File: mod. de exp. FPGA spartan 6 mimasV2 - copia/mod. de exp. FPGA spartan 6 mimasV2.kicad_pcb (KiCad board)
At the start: 2 copper layers, 111.5 x 57.8 mm, 46 parts, among them J1 locked, J2 locked, J3 locked, J4 locked, SW1 SW_DIP_x08, SW2 SW_Push, SW3 SW_Push, SW4 SW_Push, SW5 SW_Push, U1 CA56-12CGKWA

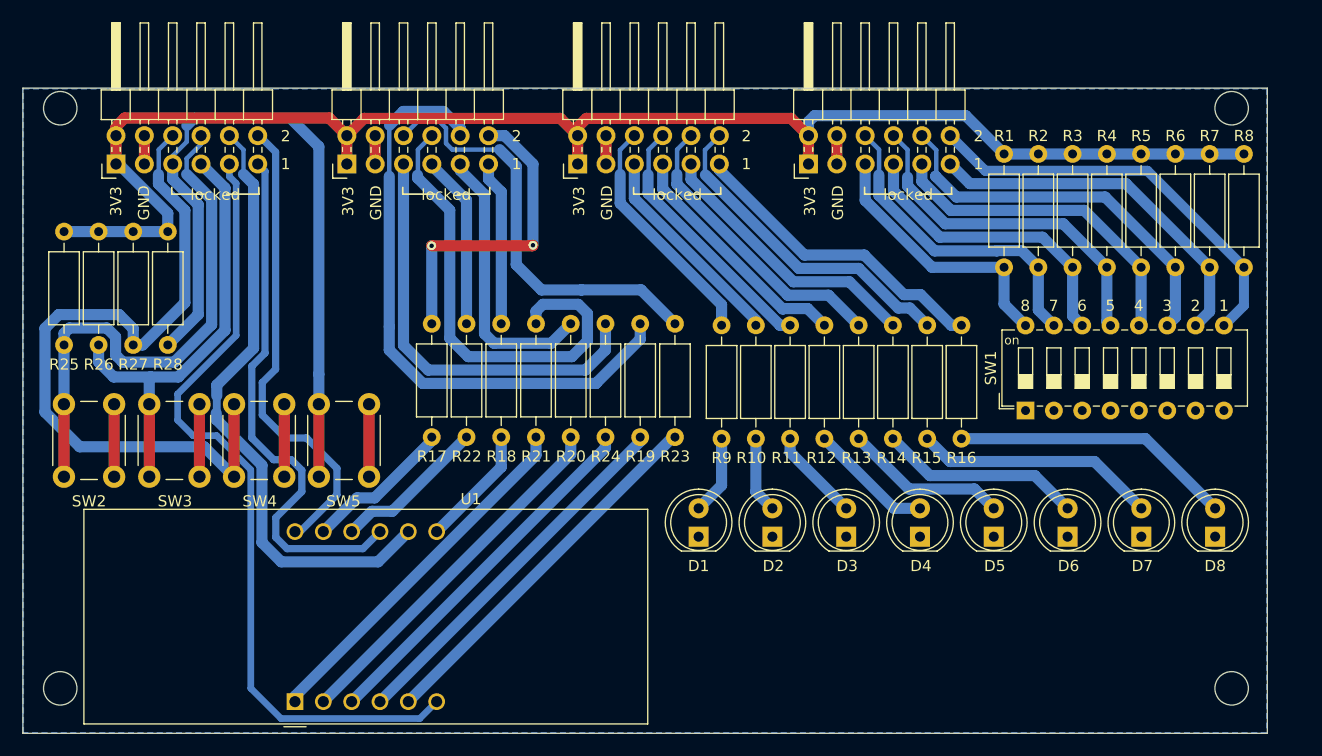
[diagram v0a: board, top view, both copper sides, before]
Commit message: el THT del FPGA modul
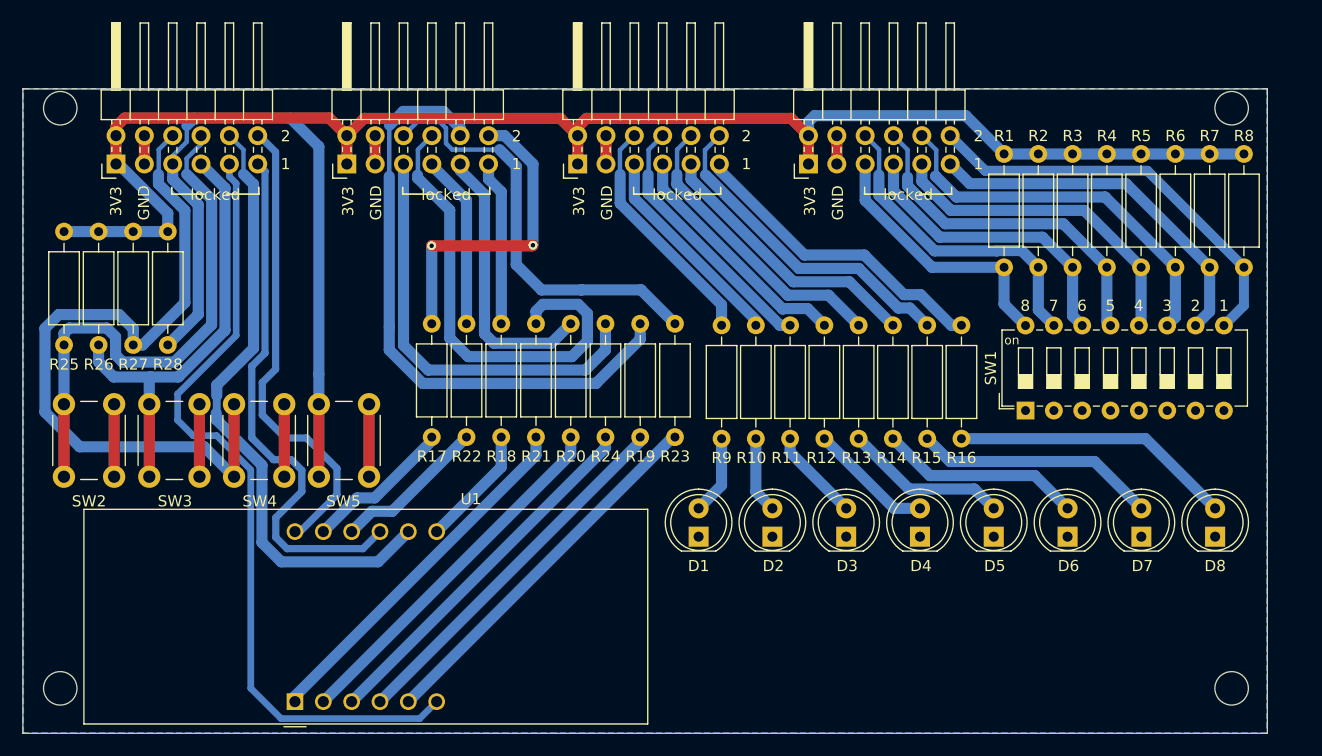
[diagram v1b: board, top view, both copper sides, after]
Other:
- outline, holes or cut-outs redrawn
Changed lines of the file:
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@@
   (gr_circle (center 200 95) (end 201.5 95) (layer "Edge.Cuts") (width 0.1) (fill none))
   (gr_circle (center 95 147) (end 96.5 147) (layer "Edge.Cuts") (width 0.1) (fill none))
-  (gr_rect (start 91.65 151.03) (end 203.2 93.2) (layer "Edge.Cuts") (width 0.1) (fill none))
+  (gr_rect (start 91.65 151.03) (end 203.2 93.27) (layer "Edge.Cuts") (width 0.1) (fill none))
   (gr_circle (center 95 95) (end 96.5 95) (layer "Edge.Cuts") (width 0.1) (fill none))
   (gr_circle (center 200 147) (end 201.5 147) (layer "Edge.Cuts") (width 0.1) (fill none))

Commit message: absolutamente todo
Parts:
- added G***: LOGO, wao:logo v2, F.Cu at (175.3, 123.0)
- R10, R11, R12, R13, R14, R15, R16, R25, R26, R27, R28, R9: footprint Resistor_THT:R_Axial_DIN0207_L6.3mm_D2.5mm_P10.16mm_Horizontal -> Resistor_THT:R_Axial_DIN0207_L6.3mm_D2.5mm_P7.62mm_Horizontal
- R17, R18, R19, R20, R21, R22, R23, R24: footprint Resistor_THT:R_Axial_DIN0207_L6.3mm_D2.5mm_P10.16mm_Horizontal -> Resistor_THT:R_Axial_DIN0207_L6.3mm_D2.5mm_P7.62mm_Horizontal; moved to B.Cu
- moved R25 26.4 mm to (110.5, 127.7)
- moved U1 26.3 mm to (110.8, 122.4)
- moved R24 24.9 mm to (119.1, 111.6)
- moved R26 23.5 mm to (107.5, 127.7)
- moved R28 21.9 mm to (101.3, 127.7)
- moved R27 21.9 mm to (104.4, 127.7)
- moved SW2 19.5 mm to (118.1, 128.4)
- moved SW4 19.5 mm to (133.3, 128.4)
- moved SW3 19.5 mm to (125.7, 128.4)
- moved SW5 19.5 mm to (140.9, 128.4)
- moved R20 15.7 mm to (125.3, 111.6)
- moved R19 12.7 mm to (134.5, 111.6)
- moved R23 9.77 mm to (140.7, 111.6)
- moved R22 9.59 mm to (122.2, 111.6)
- moved R15 9.11 mm to (163.6, 114.0)
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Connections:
- D1 pad 1: GND -> GND2
- D2 pad 1: GND -> GND2
- D3 pad 1: GND -> GND2
- D4 pad 1: GND -> GND2
- D5 pad 1: GND -> GND2
- D6 pad 1: GND -> GND2
- D7 pad 1: GND -> GND2
- D8 pad 1: GND -> GND2
- J2 pad 1: +3V3 -> +3.3V
- J2 pad 2: +3V3 -> +3.3V
- J2 pad 3: GND -> GND1
- J2 pad 4: GND -> GND1
- J3 pad 1: +3V3 -> +3.3VA
- J3 pad 2: +3V3 -> +3.3VA
- J3 pad 3: GND -> GND2
- J3 pad 4: GND -> GND2
- J4 pad 1: +3V3 -> +3.3VADC
- J4 pad 2: +3V3 -> +3.3VADC
- J4 pad 3: GND -> GND3
- J4 pad 4: GND -> GND3
- R1 pad 1: +3V3 -> +3.3VADC
- R1 pad 2: /DIP_SWITCH/7P9 -> /DIP_SWITCH/8P9
- R17 pad 1: /DISPLAY/2P7 -> /DISPLAY/1P7
- R18 pad 1: /DISPLAY/1P7 -> /DISPLAY/2P7
- R19 pad 1: /DISPLAY/4P7 -> /DISPLAY/3P7
- R2 pad 1: +3V3 -> +3.3VADC
- R2 pad 2: /DIP_SWITCH/8P9 -> /DIP_SWITCH/7P9
- R20 pad 1: /DISPLAY/3P7 -> /DISPLAY/4P7
- R21 pad 1: /DISPLAY/6P7 -> /DISPLAY/5P7
- R22 pad 1: /DISPLAY/5P7 -> /DISPLAY/6P7
- R23 pad 1: /DISPLAY/8P7 -> /DISPLAY/7P7
- R24 pad 1: /DISPLAY/7P7 -> /DISPLAY/8P7
- R3 pad 1: +3V3 -> +3.3VADC
- R3 pad 2: /DIP_SWITCH/5P9 -> /DIP_SWITCH/6P9
- R4 pad 1: +3V3 -> +3.3VADC
- R4 pad 2: /DIP_SWITCH/6P9 -> /DIP_SWITCH/5P9
- R5 pad 1: +3V3 -> +3.3VADC
- R5 pad 2: /DIP_SWITCH/3P9 -> /DIP_SWITCH/4P9
- R6 pad 1: +3V3 -> +3.3VADC
- R6 pad 2: /DIP_SWITCH/4P9 -> /DIP_SWITCH/3P9
- R7 pad 1: +3V3 -> +3.3VADC
- R7 pad 2: /DIP_SWITCH/1P9 -> /DIP_SWITCH/2P9
- R8 pad 1: +3V3 -> +3.3VADC
- R8 pad 2: /DIP_SWITCH/2P9 -> /DIP_SWITCH/1P9
- SW1 pad 1: GND -> GND3
- SW1 pad 10: /DIP_SWITCH/1P9 -> /DIP_SWITCH/2P9
- SW1 pad 11: /DIP_SWITCH/4P9 -> /DIP_SWITCH/3P9
- SW1 pad 12: /DIP_SWITCH/3P9 -> /DIP_SWITCH/4P9
- SW1 pad 13: /DIP_SWITCH/6P9 -> /DIP_SWITCH/5P9
- SW1 pad 14: /DIP_SWITCH/5P9 -> /DIP_SWITCH/6P9
- SW1 pad 15: /DIP_SWITCH/8P9 -> /DIP_SWITCH/7P9
- SW1 pad 16: /DIP_SWITCH/7P9 -> /DIP_SWITCH/8P9
- SW1 pad 2: GND -> GND3
- SW1 pad 3: GND -> GND3
- SW1 pad 4: GND -> GND3
- SW1 pad 5: GND -> GND3
- SW1 pad 6: GND -> GND3
- SW1 pad 7: GND -> GND3
- SW1 pad 8: GND -> GND3
- SW1 pad 9: /DIP_SWITCH/2P9 -> /DIP_SWITCH/1P9
- SW2 pad 1: GND -> GND2
- SW3 pad 1: GND -> GND2
- SW4 pad 1: GND -> GND2
- SW5 pad 1: GND -> GND2
- U1 pad 12: /DISPLAY/2P6 -> /DISPLAY/4P6
- U1 pad 6: /DISPLAY/3P6 -> /DISPLAY/1P6
- U1 pad 8: /DISPLAY/4P6 -> /DISPLAY/2P6
- U1 pad 9: /DISPLAY/1P6 -> /DISPLAY/3P6
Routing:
- net GND2: track 0.00 -> 147.3 mm
- net +3V3: track 136.4 -> 40.0 mm
- net +3.3VADC: track 0.00 -> 65.0 mm, vias 0 -> 1
- net /DISPLAY/3P6: track 71.8 -> 12.7 mm
- net GND3: track 0.00 -> 44.1 mm, vias 0 -> 1
- net Net-(U1-b): track 10.9 -> 53.6 mm, vias 0 -> 2
- net Net-(U1-a): track 13.4 -> 52.1 mm, vias 0 -> 2
- net /PIN_HEADER_8X4/8P6: track 66.4 -> 103.4 mm
- net /DISPLAY/4P6: track 55.4 -> 21.0 mm, vias 0 -> 2
- net GND: track 36.2 -> 2.54 mm
- net Net-(U1-DPX): track 33.1 -> 4.55 mm
- net /DISPLAY/2P6: track 42.4 -> 14.2 mm
- net /PIN_HEADER_8X4/6P6: track 48.3 -> 73.7 mm
- net /DISPLAY/4P7: track 55.1 -> 30.5 mm
- net /DIP_SWITCH/6P9: track 31.3 -> 53.4 mm
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- removed copper zone on B.Cu, net GND
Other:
- board size 111.5 x 57.8 mm -> 114.4 x 45.5 mm
- board text added: "MODULO DE EXPANSION FPGA SPARTAN_6 MIMAS-V2 PROTOTIPO V1"
